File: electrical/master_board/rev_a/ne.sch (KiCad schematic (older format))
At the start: 0 parts

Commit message: Generate Sonar footprints; added a bunch of untracked files that should be tracked.
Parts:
- added CN60: HR2_EncoderMate;HR2EncoderMate, FOOTPRINT, symbol hr2:HR2_EncoderMate;HR2EncoderMate
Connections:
- no-connect marks 0 -> 7
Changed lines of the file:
@@
 Comment4 ""
 $EndDescr
+$Comp
+L hr2:HR2_EncoderMate;HR2EncoderMate CN60
+U 1 1 5EE634C8
+P 3700 2900
+F 0 "CN60" H 4256 3190 60  0000 C CNN
+F 1 "HR2_EncoderMate;HR2EncoderMate" H 4256 3084 60  0000 C CNN
+F 2 "FOOTPRINT" H 3900 2950 60  0001 L CNN
+F 3 "HR2 Encoder Mating Connector" H 3900 2750 60  0001 L CNN
+F 4 "HR2 Encoder Mating Connector" H 3900 2650 60  0001 L CNN "Field5"
+	1    3700 2900
+	1    0    0    -1
+$EndComp
+NoConn ~ 4600 2900
+NoConn ~ 4600 3000
+NoConn ~ 4600 3100
+NoConn ~ 4600 3200
+NoConn ~ 4600 3300
+NoConn ~ 4600 3400
+NoConn ~ 4500 2750
 $EndSCHEMATC

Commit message: Have generated/footprint symbol in a KiCad project.
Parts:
- removed CN60: HR2_EncoderMate;HR2EncoderMate, FOOTPRINT, symbol hr2:HR2_EncoderMate;HR2EncoderMate
- added CN60: HCSR04H;F1X4, HR2:HCSR04_F1x4H_MATE, symbol HR2:HCSR04H;F1X4
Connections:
- no-connect marks 7 -> 4
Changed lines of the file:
@@
 Comment4 ""
 $EndDescr
+NoConn ~ 5500 3250
+NoConn ~ 5500 3350
+NoConn ~ 5500 3450
+NoConn ~ 5500 3550
 $Comp
-L hr2:HR2_EncoderMate;HR2EncoderMate CN60
-U 1 1 5EE634C8
-P 3700 2900
-F 0 "CN60" H 4256 3190 60  0000 C CNN
-F 1 "HR2_EncoderMate;HR2EncoderMate" H 4256 3084 60  0000 C CNN
-F 2 "FOOTPRINT" H 3900 2950 60  0001 L CNN
-F 3 "HR2 Encoder Mating Connector" H 3900 2750 60  0001 L CNN
-F 4 "HR2 Encoder Mating Connector" H 3900 2650 60  0001 L CNN "Field5"
-	1    3700 2900
+L HR2:HCSR04H;F1X4 CN60
+U 1 1 5EE6BF38
+P 4800 3250
+F 0 "CN60" H 5050 3400 50  0000 C CNN
+F 1 "HCSR04H;F1X4" H 5150 2800 50  0000 C CNN
+F 2 "HR2:HCSR04_F1x4H_MATE" H 5000 3300 60  0001 L CNN
+F 3 "https://cdn.sparkfun.com/datasheets/Sensors/Proximity/HCSR04.pdf" H 5000 3100 60  0001 L CNN
+F 4 "https://cdn.sparkfun.com/datasheets/Sensors/Proximity/HCSR04.pdf" H 5000 3200 60  0001 L CNN "manf#"
+F 5 "HC-SR04 Sonar (High Profile Receptacle)" H 5000 3000 60  0001 L CNN "Field5"
+	1    4800 3250
 	1    0    0    -1
 $EndComp
-NoConn ~ 4600 2900
-NoConn ~ 4600 3000
-NoConn ~ 4600 3100
-NoConn ~ 4600 3200
-NoConn ~ 4600 3300
-NoConn ~ 4600 3400
-NoConn ~ 4500 2750
 $EndSCHEMATC

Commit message: Another manually generate ne.kicad_pcb for debugging purposes.
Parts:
- CN60: value HCSR04H;F1X4 -> HCSR04;F1X4H; footprint HR2:HCSR04_F1x4H_MATE -> HR2:HCSR04_F1x4H
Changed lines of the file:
@@
 U 1 1 5EE6BF38
 P 4800 3250
-F 0 "CN60" H 5050 3400 50  0000 C CNN
-F 1 "HCSR04H;F1X4" H 5150 2800 50  0000 C CNN
-F 2 "HR2:HCSR04_F1x4H_MATE" H 5000 3300 60  0001 L CNN
+F 0 "CN60" H 5100 3400 50  0000 C CNN
+F 1 "HCSR04;F1X4H" H 5150 2800 50  0000 C CNN
+F 2 "HR2:HCSR04_F1x4H" H 5000 3300 60  0001 L CNN
 F 3 "https://cdn.sparkfun.com/datasheets/Sensors/Proximity/HCSR04.pdf" H 5000 3100 60  0001 L CNN
 F 4 "https://cdn.sparkfun.com/datasheets/Sensors/Proximity/HCSR04.pdf" H 5000 3200 60  0001 L CNN "manf#"

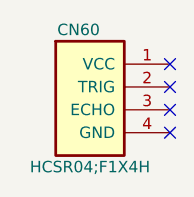
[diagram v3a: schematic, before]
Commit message: Successfully placed a font surface non-rotated footprint in ne.kicad_pcb.
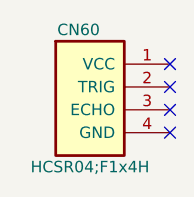
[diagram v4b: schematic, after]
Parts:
- CN60: value HCSR04;F1X4H -> HCSR04;F1x4H
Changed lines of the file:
@@
 P 4800 3250
 F 0 "CN60" H 5100 3400 50  0000 C CNN
-F 1 "HCSR04;F1X4H" H 5150 2800 50  0000 C CNN
+F 1 "HCSR04;F1x4H" H 5150 2800 50  0000 C CNN
 F 2 "HR2:HCSR04_F1x4H" H 5000 3300 60  0001 L CNN
 F 3 "https://cdn.sparkfun.com/datasheets/Sensors/Proximity/HCSR04.pdf" H 5000 3100 60  0001 L CNN

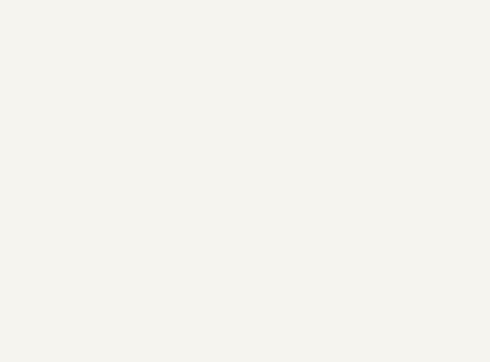
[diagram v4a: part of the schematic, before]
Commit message: Added spacer mounting holes to schematics and associated PCB's.
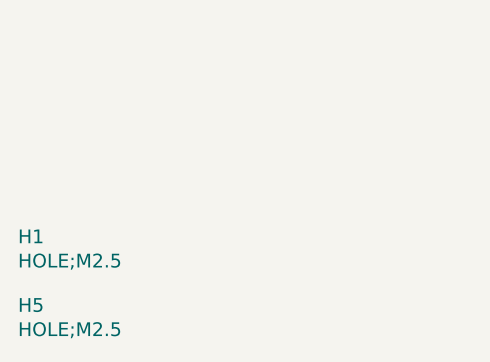
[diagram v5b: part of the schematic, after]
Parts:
- added H1, H5: HOLE;M2.5, MountingHole:MountingHole_2.7mm_M2.5, symbol HR2:HOLE;M2.5
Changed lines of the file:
@@
+	1    0    0    -1
+$EndComp
+$Comp
+L HR2:HOLE;M2.5 H5
+U 1 1 5F2F7E7C
+P 1800 4850
+F 0 "H5" H 1825 4903 60  0000 L CNN
+F 1 "HOLE;M2.5" H 1825 4797 60  0000 L CNN
+F 2 "MountingHole:MountingHole_2.7mm_M2.5" H 2000 4900 60  0001 L CNN
+F 3 "M2.5 Mounting Hole" H 2000 4700 60  0001 L CNN
+	1    1800 4850
+	1    0    0    -1
+$EndComp
+$Comp
+L HR2:HOLE;M2.5 H1
+U 1 1 5F2F85AA
+P 1800 4550
+F 0 "H1" H 1825 4603 60  0000 L CNN
+F 1 "HOLE;M2.5" H 1825 4497 60  0000 L CNN
+F 2 "MountingHole:MountingHole_2.7mm_M2.5" H 2000 4600 60  0001 L CNN
+F 3 "M2.5 Mounting Hole" H 2000 4400 60  0001 L CNN
+	1    1800 4550
 	1    0    0    -1
 $EndComp

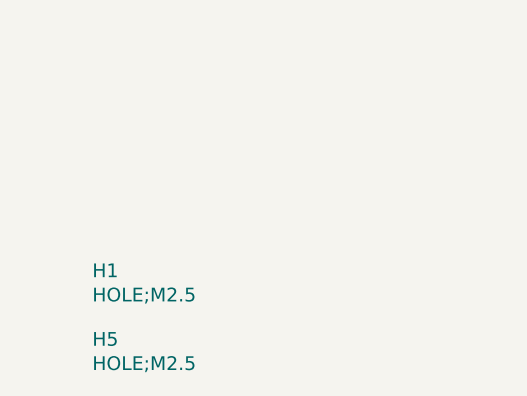
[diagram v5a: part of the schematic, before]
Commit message: Placed all of the Groves on the PCB's.
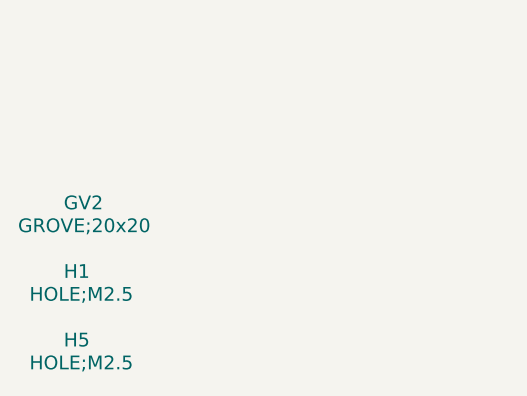
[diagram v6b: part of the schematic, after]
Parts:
- added GV2: GROVE;20x20, HR2:GROVE20x20, symbol HR2:GROVE;20x20
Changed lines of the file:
@@
 U 1 1 5F2F7E7C
 P 1800 4850
-F 0 "H5" H 1825 4903 60  0000 L CNN
-F 1 "HOLE;M2.5" H 1825 4797 60  0000 L CNN
+F 0 "H5" H 1700 4900 60  0000 L CNN
+F 1 "HOLE;M2.5" H 1550 4800 60  0000 L CNN
 F 2 "MountingHole:MountingHole_2.7mm_M2.5" H 2000 4900 60  0001 L CNN
 F 3 "M2.5 Mounting Hole" H 2000 4700 60  0001 L CNN
@@
 U 1 1 5F2F85AA
 P 1800 4550
-F 0 "H1" H 1825 4603 60  0000 L CNN
-F 1 "HOLE;M2.5" H 1825 4497 60  0000 L CNN
+F 0 "H1" H 1700 4600 60  0000 L CNN
+F 1 "HOLE;M2.5" H 1550 4500 60  0000 L CNN
 F 2 "MountingHole:MountingHole_2.7mm_M2.5" H 2000 4600 60  0001 L CNN
 F 3 "M2.5 Mounting Hole" H 2000 4400 60  0001 L CNN
@@
 	1    0    0    -1
 $EndComp
+$Comp
+L HR2:GROVE;20x20 GV2
+U 1 1 5F2F9731
+P 1800 4250
+F 0 "GV2" H 1700 4300 60  0000 L CNN
+F 1 "GROVE;20x20" H 1500 4200 60  0000 L CNN
+F 2 "HR2:GROVE20x20" H 2000 4300 60  0001 L CNN
+F 3 "Grove 20x20 Module" H 2000 4100 60  0001 L CNN
+F 4 "Grove 20x20 Module" H 2000 4200 60  0001 L CNN "manf#"
+	1    1800 4250
+	1    0    0    -1
+$EndComp

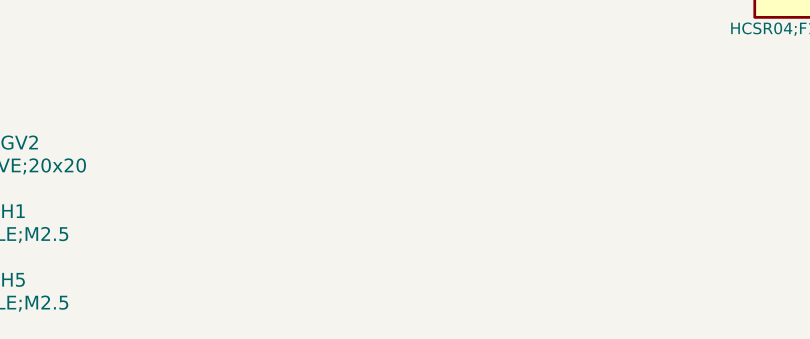
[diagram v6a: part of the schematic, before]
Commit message: Added LED's to the PCB's.
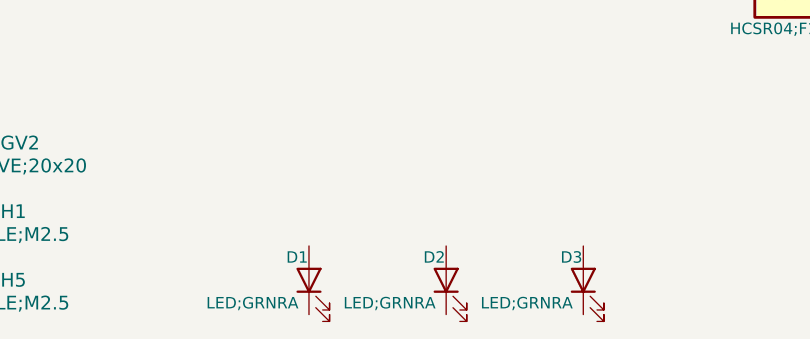
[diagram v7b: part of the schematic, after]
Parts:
- added D1, D2, D3: LED;GRNRA, HR2:LED_GRNRA, symbol Device:LED
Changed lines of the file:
@@
 	1    0    0    -1
 $EndComp
+$Comp
+L Device:LED D1
+U 1 1 5F30B259
+P 3050 4800
+F 0 "D1" V 3150 4900 50  0000 R CNN
+F 1 "LED;GRNRA" V 2950 5250 50  0000 R CNN
+F 2 "HR2:LED_GRNRA" H 3050 4800 50  0001 C CNN
+F 3 "~" H 3050 4800 50  0001 C CNN
+	1    3050 4800
+	0    -1   -1   0
+$EndComp
+$Comp
+L Device:LED D3
+U 1 1 5F30DE2E
+P 4250 4800
+F 0 "D3" V 4350 4900 50  0000 R CNN
+F 1 "LED;GRNRA" V 4150 5250 50  0000 R CNN
+F 2 "HR2:LED_GRNRA" H 4250 4800 50  0001 C CNN
+F 3 "~" H 4250 4800 50  0001 C CNN
+	1    4250 4800
+	0    -1   -1   0
+$EndComp
+$Comp
+L Device:LED D2
+U 1 1 5F30D43E
+P 3650 4800
+F 0 "D2" V 3750 4900 50  0000 R CNN
+F 1 "LED;GRNRA" V 3550 5250 50  0000 R CNN
+F 2 "HR2:LED_GRNRA" H 3650 4800 50  0001 C CNN
+F 3 "~" H 3650 4800 50  0001 C CNN
+	1    3650 4800
+	0    -1   -1   0
+$EndComp
 $EndSCHEMATC

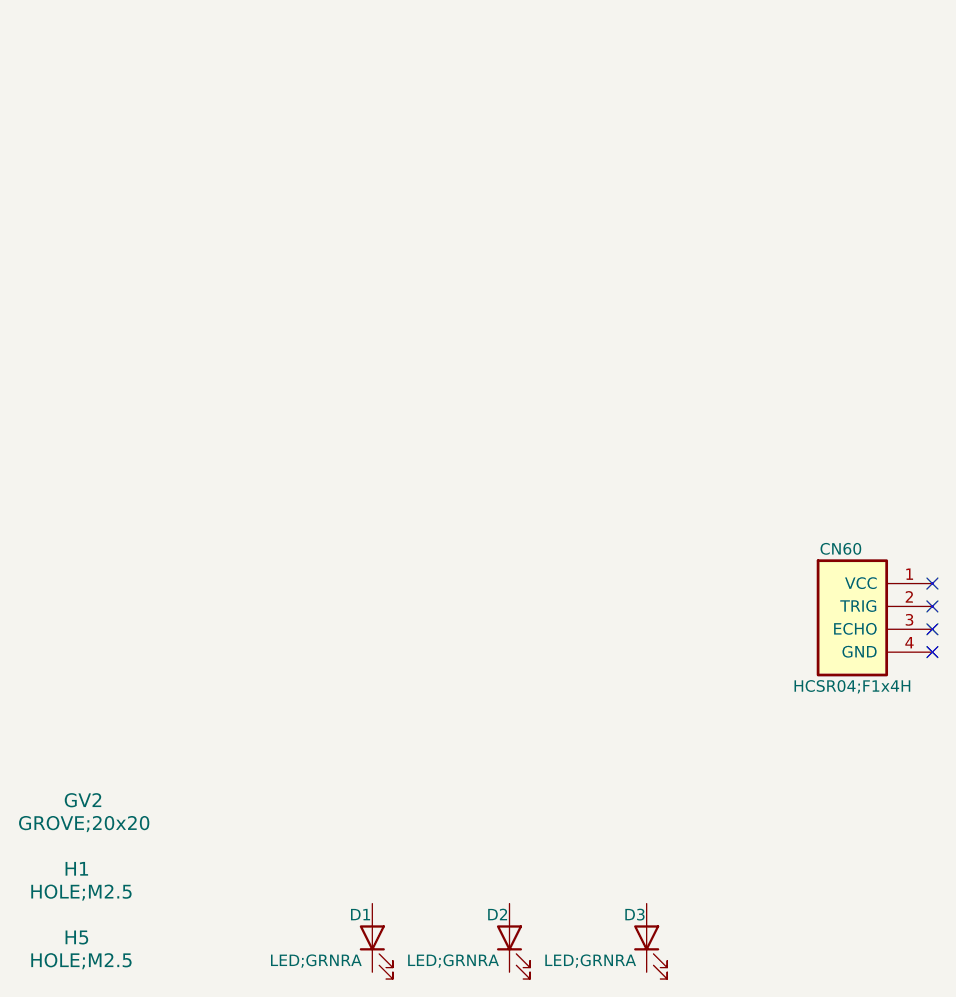
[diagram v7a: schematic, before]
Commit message: Got Bridge connectors installed on PCB's. Tweaking still required.
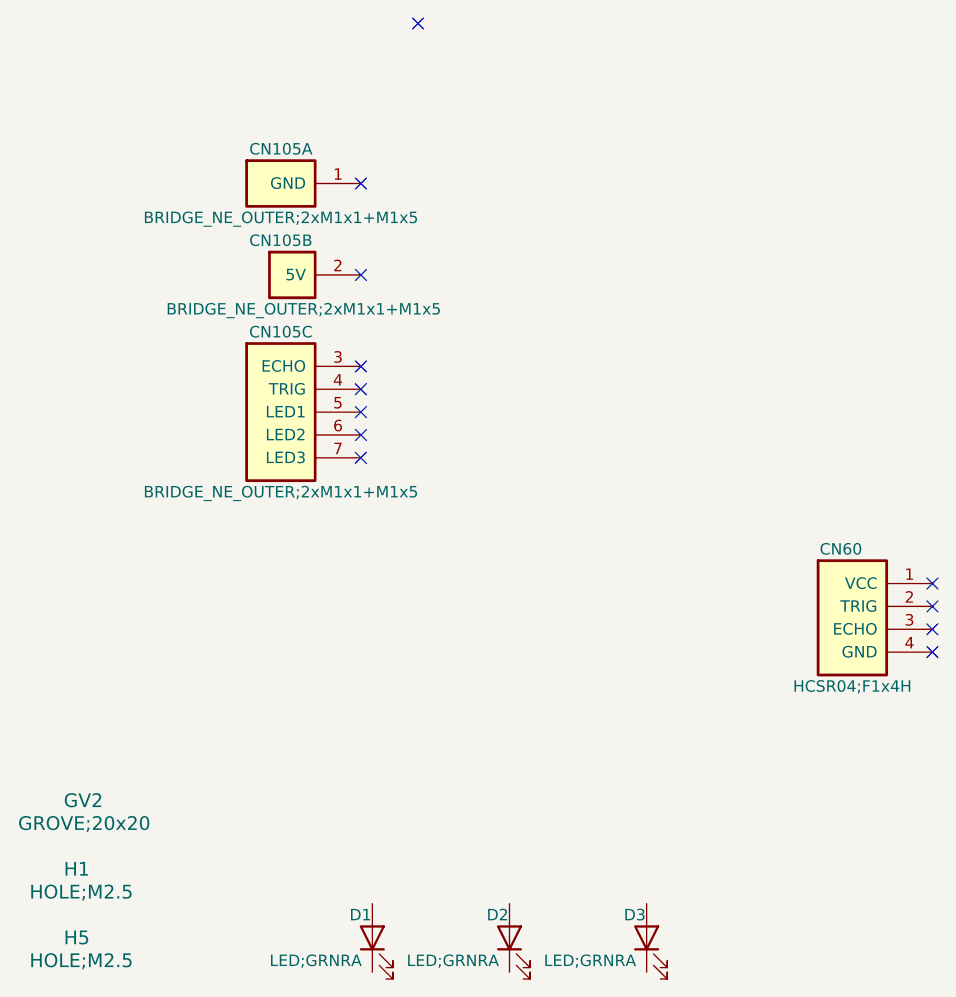
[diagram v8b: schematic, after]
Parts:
- added CN105: BRIDGE_NE_OUTER;2xM1x1+M1x5, HR2:BRIDGE_NE_OUTER_2xM1x1+M1x5, symbol HR2:BRIDGE_NE_OUTER;2xM1x1+M1x5
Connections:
- no-connect marks 4 -> 12
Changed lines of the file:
@@
 	0    -1   -1   0
 $EndComp
+$Comp
+L HR2:BRIDGE_NE_OUTER;2xM1x1+M1x5 CN105
+U 1 1 5F387457
+P 2300 1500
+F 0 "CN105" H 2650 1650 50  0000 C CNN
+F 1 "BRIDGE_NE_OUTER;2xM1x1+M1x5" H 2650 1350 50  0000 C CNN
+F 2 "HR2:BRIDGE_NE_OUTER_2xM1x1+M1x5" H 2500 1550 60  0001 L CNN
+F 3 "" H 2500 1350 60  0001 L CNN
+F 4 "NE Outer Bridge Connectors" H 2500 1250 60  0001 L CNN "Field5"
+	1    2300 1500
+	1    0    0    -1
+$EndComp
+$Comp
+L HR2:BRIDGE_NE_OUTER;2xM1x1+M1x5 CN105
+U 2 1 5F38833D
+P 2400 1900
+F 0 "CN105" H 2650 2050 50  0000 C CNN
+F 1 "BRIDGE_NE_OUTER;2xM1x1+M1x5" H 2750 1750 50  0000 C CNN
+F 2 "HR2:BRIDGE_NE_OUTER_2xM1x1+M1x5" H 2600 1950 60  0001 L CNN
+F 3 "" H 2600 1750 60  0001 L CNN
+F 4 "NE Outer Bridge Connectors" H 2600 1650 60  0001 L CNN "Field5"
+	2    2400 1900
+	1    0    0    -1
+$EndComp
+$Comp
+L HR2:BRIDGE_NE_OUTER;2xM1x1+M1x5 CN105
+U 3 1 5F3890E6
+P 2300 2300
+F 0 "CN105" H 2650 2450 50  0000 C CNN
+F 1 "BRIDGE_NE_OUTER;2xM1x1+M1x5" H 2650 1750 50  0000 C CNN
+F 2 "HR2:BRIDGE_NE_OUTER_2xM1x1+M1x5" H 2500 2350 60  0001 L CNN
+F 3 "" H 2500 2150 60  0001 L CNN
+F 4 "NE Outer Bridge Connectors" H 2500 2050 60  0001 L CNN "Field5"
+	3    2300 2300
+	1    0    0    -1
+$EndComp
+NoConn ~ 3000 1500
+NoConn ~ 3000 1900
+NoConn ~ 3000 2300
+NoConn ~ 3000 2400
+NoConn ~ 3000 2500
+NoConn ~ 3000 2600
+NoConn ~ 3000 2700
+NoConn ~ 3250 800
 $EndSCHEMATC
